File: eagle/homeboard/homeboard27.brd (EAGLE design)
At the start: 94 x 71.8 mm, 124 parts, among them IC1 XCF02S, IC2 25LC080SN, IC3 ATMEGA32U2-TQFP, Q5 BC848SMD, Q6 BC848SMD, Q7 BC848SMD, Q8 BC848SMD, T1 BSS138, T2 BC848, T3 BSS138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

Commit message: crap, how late is it now...
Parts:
- moved R50 9.80 mm to (40.8, 18.2), turned to 90 degrees
- moved C14 1.12 mm to (46.0, 21.0), turned to 0 degrees
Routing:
- net GND: track 991.2 -> 1007.3 mm, vias 67 -> 70
- net SCART_BLANKING: track 18.8 -> 29.0 mm
- net VCCAUX: track 123.7 -> 122.7 mm
- net VCC: track 543.3 -> 544.3 mm

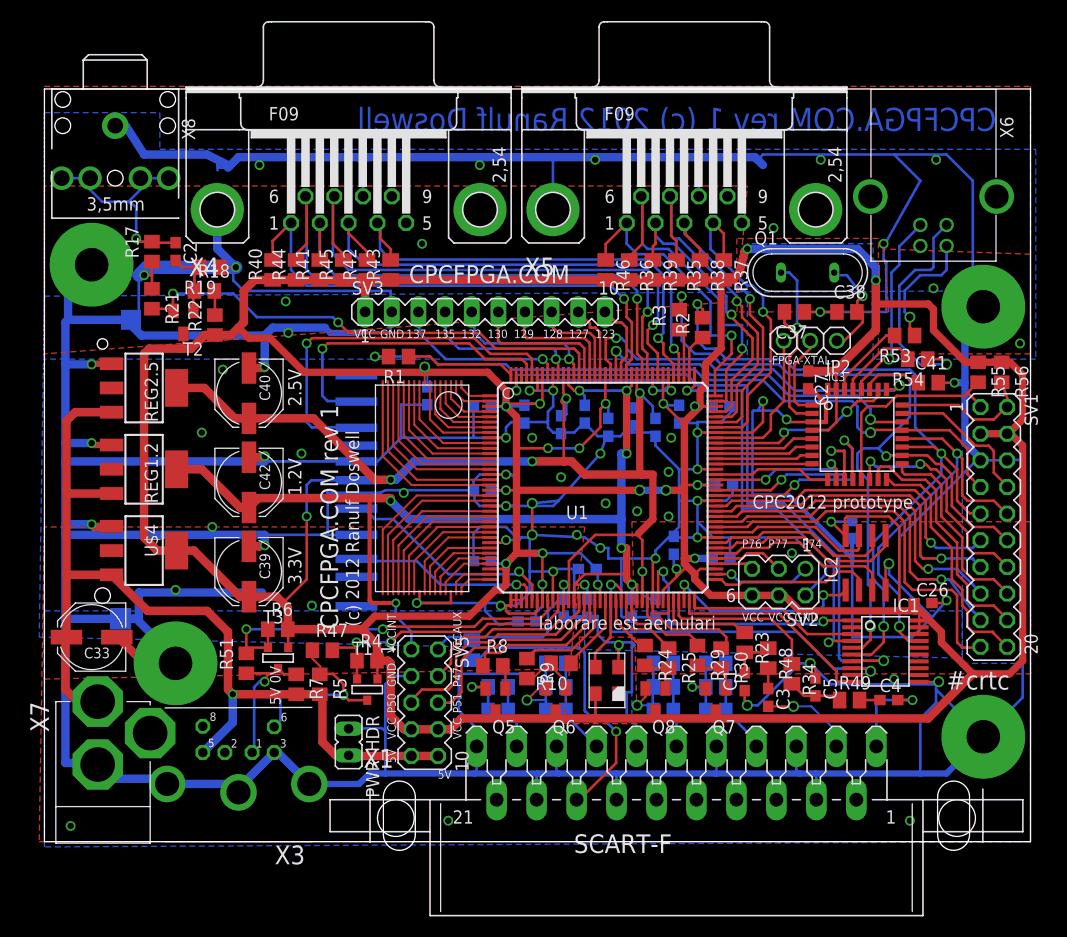
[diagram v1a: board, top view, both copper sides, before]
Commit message: added led
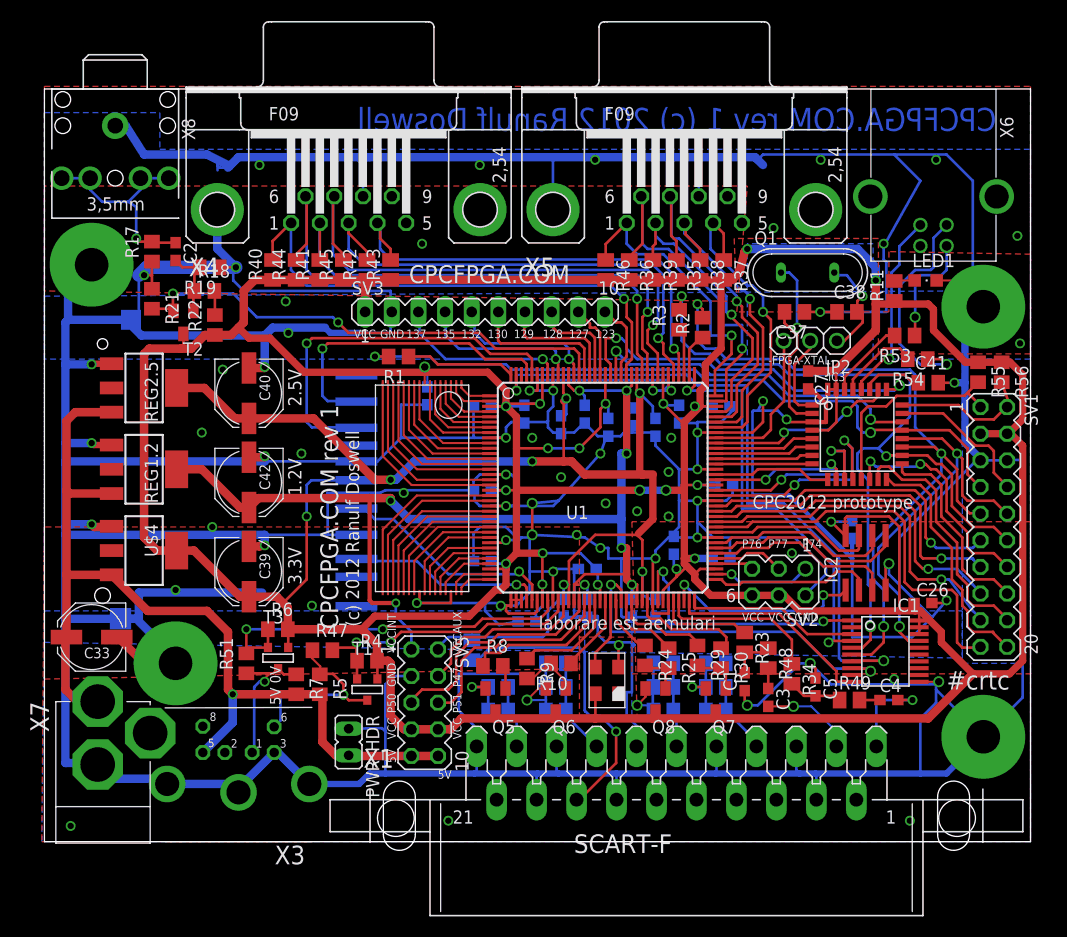
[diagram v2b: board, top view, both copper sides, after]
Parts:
- added LED1: (no value), adafruit:CHIPLED_0805
- added R11: (no value), resistor:M0805
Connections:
- new net N$10: LED1.A, R11.2
- net GND: now also LED1.C
- net VCC: now also R11.1
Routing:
- net GND: track 1007.3 -> 1012.8 mm
- net N$10: track 0.00 -> 2.00 mm
- net N$36: track 11.8 -> 11.0 mm
- net VCC: track 544.3 -> 544.8 mm
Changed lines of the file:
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@@
 <attribute name="OC_FARNELL" value="unknown" x="90.5" y="30" size="1.778" layer="27" rot="R270" display="off"/>
 </element>
+<element name="R11" library="resistor" package="M0805" value="" x="81" y="52.5" rot="R90"/>
+<element name="LED1" library="adafruit" package="CHIPLED_0805" value="" x="84" y="53.5" rot="R270"/>
 </elements>
 <signals>
@@
 <vertex x="11" y="69.5"/>
 <vertex x="11" y="66"/>
-<vertex x="94.5" y="66"/>
-<vertex x="94.5" y="46"/>
+<vertex x="94" y="66"/>
+<vertex x="94" y="46"/>
 <vertex x="79" y="46"/>
 <vertex x="79" y="57"/>
@@
 <vertex x="94" y="22"/>
 <vertex x="94" y="0"/>
-<vertex x="0" y="-0.5"/>
+<vertex x="-0.25" y="0"/>
 </polygon>
 <polygon width="0.4064" layer="16" isolate="0.55" orphans="yes">
 <vertex x="87.5" y="52.5"/>
 <vertex x="0" y="52"/>
-<vertex x="-0.5" y="19.5"/>
+<vertex x="0" y="19"/>
 <vertex x="87.5" y="17.5"/>
 </polygon>
@@
 <vertex x="79.5" y="46.5"/>
 <vertex x="79.5" y="57.5"/>
-<vertex x="66" y="57.5"/>
+<vertex x="65.75" y="57.5"/>
 <vertex x="66" y="51.5"/>
-<vertex x="0" y="46.5"/>
+<vertex x="0" y="52.5"/>
 </polygon>
 <polygon width="0.4064" layer="1" isolate="0.55" orphans="yes">
 <vertex x="94" y="30.5"/>
 <vertex x="56" y="30.5"/>
-<vertex x="56.5" y="11.25"/>
-<vertex x="49.5" y="11.25"/>
-<vertex x="51.5" y="30"/>
+<vertex x="56.5" y="11.75"/>
+<vertex x="51" y="11.75"/>
+<vertex x="51" y="30"/>
 <vertex x="0" y="30"/>
-<vertex x="-0.5" y="0"/>
+<vertex x="-0.25" y="0"/>
 <vertex x="94" y="0"/>
 </polygon>
 <polygon width="0.4064" layer="1" isolate="0.55" orphans="yes">
 <vertex x="94" y="56"/>
-<vertex x="80" y="56.5"/>
+<vertex x="80.5" y="56.25"/>
 <vertex x="80.5" y="50.5"/>
 <vertex x="66" y="50.5"/>
@@
 <via x="52.5" y="65" extent="1-16" drill="0.6" shape="square"/>
 <via x="24.5" y="37" extent="1-16" drill="0.6" shape="square"/>
-<via x="84.75" y="52.75" extent="1-16" drill="0.6" shape="square"/>
+<via x="92.75" y="57.75" extent="1-16" drill="0.6" shape="square"/>
 <via x="69.5" y="58.5" extent="1-16" drill="0.6" shape="square"/>
 <via x="80" y="57" extent="1-16" drill="0.6" shape="square"/>
@@
 <via x="53.5" y="32.25" extent="1-16" drill="0.6" shape="square"/>
 <via x="50.75" y="29.25" extent="1-16" drill="0.6" shape="square"/>
+<contactref element="LED1" pad="C"/>
+<wire x1="85.05" y1="53.5" x2="87" y2="53.5" width="0.2" layer="1"/>
+<wire x1="87" y1="53.5" x2="89.5" y2="51" width="0.2" layer="1"/>
+<wire x1="86" y1="65.5" x2="85" y2="65" width="0" layer="19" extent="16-16"/>
+<wire x1="89.23" y1="36.35" x2="89.25" y2="36.25" width="0" layer="19" extent="16-16"/>
+<wire x1="60" y1="29.1" x2="60" y2="29" width="0" layer="19" extent="16-16"/>
+<wire x1="80" y1="57" x2="80" y2="56.75" width="0" layer="19" extent="16-16"/>
+<wire x1="50.75" y1="29.25" x2="51.5" y2="29" width="0" layer="19" extent="16-16"/>
+<wire x1="59.5" y1="35.25" x2="60.5" y2="35.5" width="0" layer="19" extent="16-16"/>
+<wire x1="59.75" y1="38.5" x2="58.5" y2="38.5" width="0" layer="19" extent="16-16"/>
+<wire x1="59.5" y1="31" x2="60.5" y2="30" width="0" layer="19" extent="16-16"/>
+<wire x1="71.25" y1="27.5" x2="71.5" y2="29" width="0" layer="19" extent="16-16"/>
+<wire x1="46.5" y1="38.5" x2="46.1" y2="40" width="0" layer="19" extent="16-16"/>
+<wire x1="23.25" y1="48.5" x2="21.75" y2="49" width="0" layer="19" extent="16-16"/>
+<wire x1="41.2" y1="9.08" x2="41.2" y2="10.8" width="0" layer="19" extent="16-16"/>
+<wire x1="34.25" y1="33.25" x2="32.5" y2="33.5" width="0" layer="19" extent="16-16"/>
+<wire x1="20.5" y1="64.5" x2="18.5" y2="65.25" width="0" layer="19" extent="16-16"/>
+<wire x1="49.25" y1="34.75" x2="49" y2="32.5" width="0" layer="19" extent="16-16"/>
+<wire x1="81" y1="15.5" x2="83.393396875" y2="15.237409375" width="0" layer="19" extent="1-1"/>
+<wire x1="17" y1="45" x2="19.5" y2="45.15" width="0" layer="19" extent="1-1"/>
+<wire x1="23" y1="51.5" x2="21.75" y2="49" width="0" layer="19" extent="16-16"/>
+<wire x1="56.5" y1="31.5" x2="59.5" y2="31" width="0" layer="19" extent="1-1"/>
+<wire x1="53.5" y1="32.25" x2="56.5" y2="31.5" width="0" layer="19" extent="1-1"/>
+<wire x1="24.5" y1="37" x2="21" y2="36.65" width="0" layer="19" extent="1-1"/>
+<wire x1="12.5" y1="24" x2="9" y2="23.75" width="0" layer="19" extent="16-16"/>
+<wire x1="16" y1="30" x2="19.5" y2="28.15" width="0" layer="19" extent="1-1"/>
+<wire x1="52.5" y1="65" x2="48.5" y2="65.25" width="0" layer="19" extent="16-16"/>
+<wire x1="82.5" y1="2" x2="83.5" y2="6.5" width="0" layer="19" extent="16-16"/>
+<wire x1="25.5" y1="22.5" x2="20.75" y2="23.75" width="0" layer="19" extent="16-16"/>
+<wire x1="93" y1="47.5" x2="89.5" y2="51" width="0" layer="19" extent="1-1"/>
+<wire x1="15" y1="39" x2="19.5" y2="36.65" width="0" layer="19" extent="1-1"/>
+<wire x1="38.5" y1="2" x2="41" y2="6.5" width="0" layer="19" extent="16-16"/>
+<wire x1="36" y1="57" x2="33" y2="52.5" width="0" layer="19" extent="16-16"/>
+<wire x1="74" y1="65" x2="68.5" y2="65.5" width="0" layer="19" extent="16-16"/>
+<wire x1="2.5" y1="1.5" x2="6.4318" y2="6" width="0" layer="19" extent="16-16"/>
+<wire x1="69.5" y1="58.5" x2="68.5" y2="64.5" width="0" layer="19" extent="16-16"/>
+<wire x1="92.75" y1="57.75" x2="88.5" y2="63" width="0" layer="19" extent="16-16"/>
+<wire x1="41.5" y1="64.5" x2="48.4778" y2="65.2278" width="0" layer="19" extent="16-16"/>
 </signal>
 <signal name="VCC">
@@
 <wire x1="87.8" y1="45.7" x2="84.75" y2="48.75" width="0.7" layer="1"/>
 <wire x1="84.75" y1="48.75" x2="84.75" y2="50.75" width="0.7" layer="1"/>
-<wire x1="79.25" y1="51.25" x2="84.25" y2="51.25" width="0.7" layer="1"/>
+<wire x1="79.25" y1="51.25" x2="81" y2="51.25" width="0.7" layer="1"/>
+<wire x1="81" y1="51.25" x2="84.25" y2="51.25" width="0.7" layer="1"/>
 <wire x1="84.25" y1="51.25" x2="84.75" y2="50.75" width="0.7" layer="1"/>
 <wire x1="89" y1="45.7" x2="91.25" y2="45.7" width="0.7" layer="1"/>
@@
 <wire x1="47.47" y1="22.47" x2="46.85" y2="21.85" width="0.254" layer="16"/>
 <wire x1="46.85" y1="21" x2="46.85" y2="21.85" width="0.254" layer="16"/>
+<contactref element="R11" pad="1"/>
+<wire x1="81" y1="51.55" x2="81" y2="51.5" width="0.2" layer="1"/>
+<wire x1="81" y1="51" x2="81" y2="51.25" width="0.2" layer="1"/>
+<wire x1="81" y1="51.5" x2="81" y2="51.25" width="0.2" layer="1"/>
 </signal>
 <signal name="TCK">
@@
 <wire x1="86" y1="54.5" x2="86" y2="56.79" width="0.254" layer="16"/>
 <wire x1="83" y1="48.3" x2="82.95" y2="48.25" width="0.254" layer="1"/>
-<wire x1="83.5" y1="54" x2="82" y2="52.5" width="0.254" layer="16"/>
-<wire x1="82" y1="52.5" x2="82" y2="50.5" width="0.254" layer="16"/>
-<wire x1="82" y1="50.5" x2="82.5" y2="50" width="0.254" layer="16"/>
-<via x="82.5" y="50" extent="1-16" drill="0.7" shape="square"/>
-<wire x1="82.5" y1="50" x2="82.5" y2="49" width="0.254" layer="1"/>
-<wire x1="82.5" y1="49" x2="83" y2="48.5" width="0.254" layer="1"/>
-<wire x1="83" y1="48.3" x2="83" y2="48.5" width="0.254" layer="1"/>
+<wire x1="83.5" y1="54" x2="83" y2="53.5" width="0.254" layer="16"/>
+<wire x1="83" y1="53.5" x2="83" y2="50" width="0.254" layer="16"/>
+<via x="83" y="50" extent="1-16" drill="0.7" shape="square"/>
+<wire x1="83" y1="50" x2="83" y2="48.3" width="0.254" layer="1"/>
 </signal>
 <signal name="N$66">
@@
 <wire x1="70" y1="26" x2="70" y2="26.02" width="0.254" layer="1"/>
 </signal>
+<signal name="N$10">
+<contactref element="LED1" pad="A"/>
+<contactref element="R11" pad="2"/>
+<wire x1="82.95" y1="53.5" x2="81" y2="53.5" width="0.2" layer="1"/>
+<wire x1="81" y1="53.5" x2="81" y2="53.45" width="0.2" layer="1"/>
+</signal>
 </signals>

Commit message: moved some stuff
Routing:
- net GND: track 1012.8 -> 1024.2 mm, vias 70 -> 82
- net JOY1_RIGHT: track 30.3 -> 29.0 mm
- net JOY1_UP: track 28.3 -> 27.2 mm
- net JOY1_FIRE2: track 34.2 -> 33.4 mm
- net JOY1_FIRE1: track 33.7 -> 33.0 mm
- net JOY1_LEFT: track 29.5 -> 28.9 mm
